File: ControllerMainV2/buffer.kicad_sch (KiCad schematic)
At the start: 21 parts

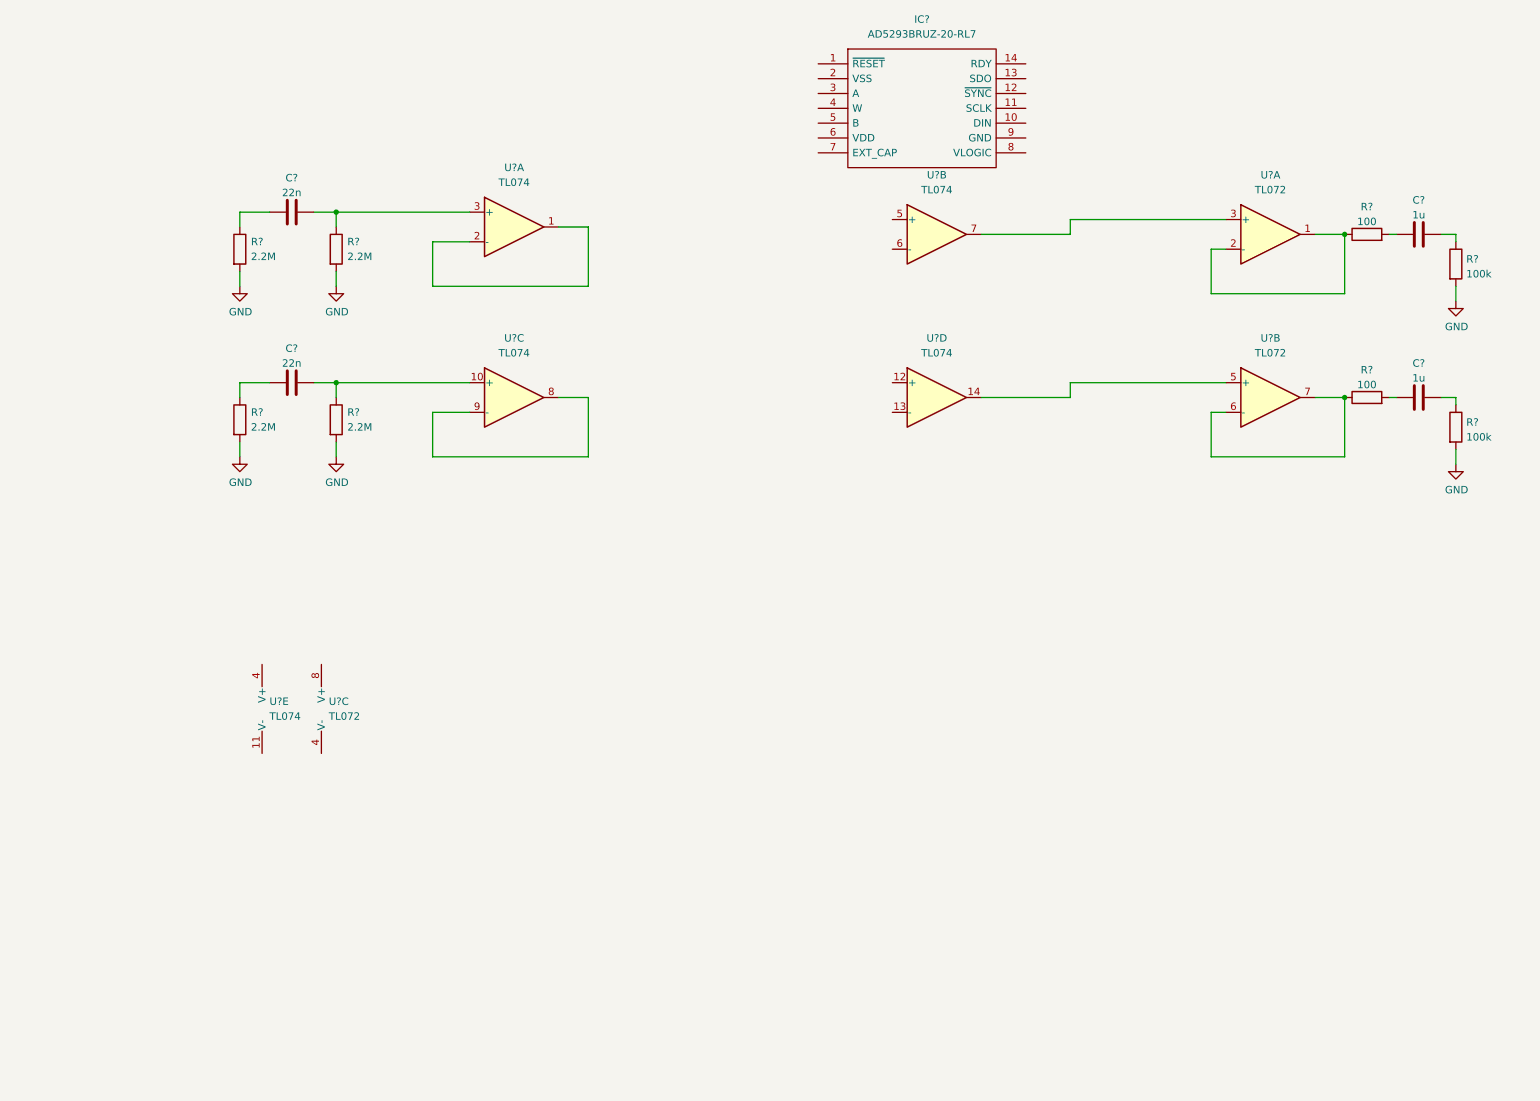
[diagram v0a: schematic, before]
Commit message: Added amp schematic
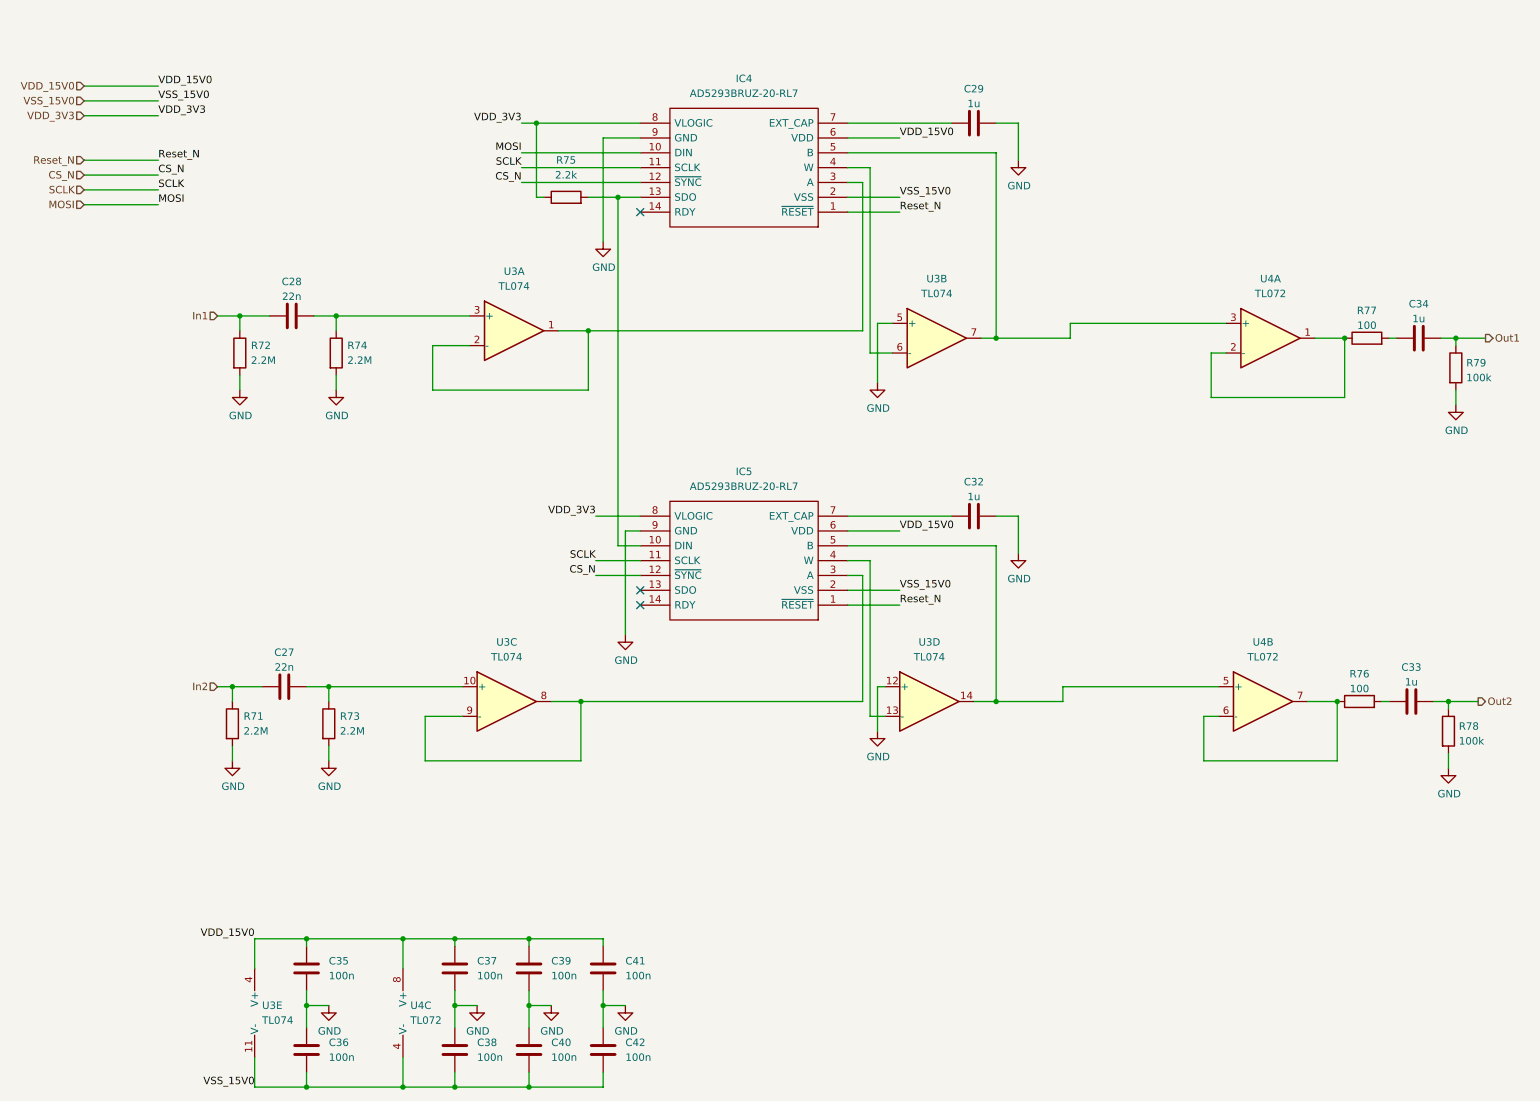
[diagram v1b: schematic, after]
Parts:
- added C29, C32: 1u, Capacitor_SMD:C_1206_3216Metric_Pad1.33x1.80mm_HandSolder, symbol Device:C
- added C35, C36, C37, C38, C39, C40, C41, C42: 100n, Capacitor_SMD:C_1206_3216Metric_Pad1.33x1.80mm_HandSolder, symbol Device:C
- added IC5: AD5293BRUZ-20-RL7, SOP65P640X120-14N, symbol SamacSys_Parts:AD5293BRUZ-20-RL7
- added R75: 2.2k, Resistor_SMD:R_1206_3216Metric_Pad1.30x1.75mm_HandSolder, symbol Device:R
- gave numbers to parts that had none: 15
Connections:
- net GND: now also IC4.9 (GND), U3.12 (+), U3.5 (+), C29.2, C32.2, C35.1, C36.2, C37.1, C38.2, C39.1, C40.2, C41.1, C42.2, IC5.9 (GND)
- net Out1: now reaches C34.2, R79.1
- net at U3.14, U4.5 (+): now also IC5.5 (B)
- net Out2: now reaches C33.2, R78.1
- net In2: now reaches C27.1, R71.1
- net at U3.6 (-): now also IC4.4 (W)
- net at U3.7, U4.3 (+): now also IC4.5 (B)
- net at U3.8, U3.9 (-): now also IC5.3 (A)
- net Reset_N: now reaches IC4.1 (~{RESET})
- net Reset_N: now also IC5.1 (~{RESET})
- net MOSI: now reaches IC4.10 (DIN)
- net SCLK: now reaches IC4.11 (SCLK)
- net SCLK: now also IC5.11 (SCLK)
- net CS_N: now reaches IC4.12 (~{SYNC})
- net CS_N: now also IC5.12 (~{SYNC})
- net at IC4.13 (SDO): now also IC5.10 (DIN), R75.2
- net VSS_15V0: now reaches IC4.2 (VSS)
- net VSS_15V0: now also U3.11 (V-), U4.4 (V-), C36.1, C38.1, C40.1, C42.1, IC5.2 (VSS)
- net at IC4.3 (A): now also U3.1, U3.2 (-)
- net VDD_15V0: now reaches IC4.6 (VDD)
- net VDD_15V0: now also U3.4 (V+), U4.8 (V+), C35.2, C37.2, C39.2, C41.2, IC5.6 (VDD)
- net at IC4.7 (EXT_CAP): now also C29.1
- net VDD_3V3: now reaches IC4.8 (VLOGIC)
- net VDD_3V3: now also IC5.8 (VLOGIC), R75.1
- net In1: now reaches C28.1, R72.1
- net at U3.13 (-): now also IC5.4 (W)
- new net: C32.1, IC5.7 (EXT_CAP)
- no-connect marks 0 -> 3
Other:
- moved on the sheet: C27, C28, C33, C34, IC4, R71, R72, R73, R74, R76, R77, R78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

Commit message: Layout of PGAs
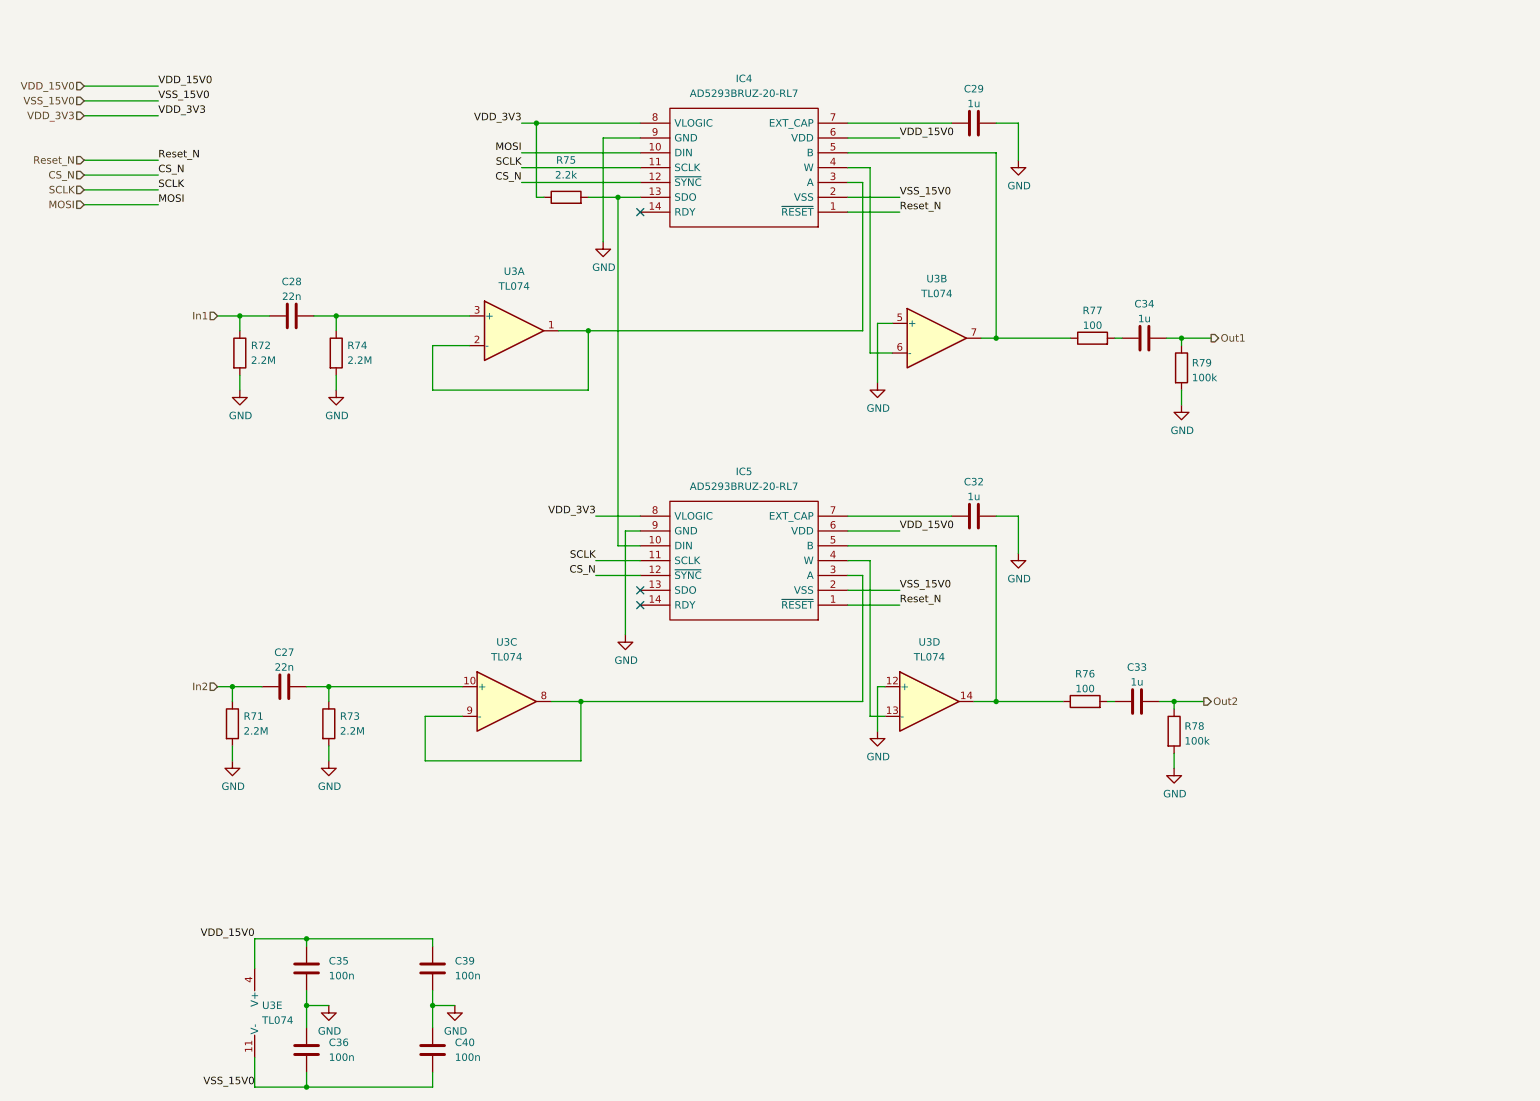
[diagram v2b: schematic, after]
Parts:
- removed C37, C38, C41, C42: 100n, Capacitor_SMD:C_1206_3216Metric_Pad1.33x1.80mm_HandSolder, symbol Device:C
- removed U4: TL072, symbol Amplifier_Operational:TL072
- IC4, IC5: footprint SOP65P640X120-14N -> SamacSys_Parts:SOP65P640X120-14N
- U3: footprint (none) -> SamacSys_Parts:SOIC127P600X175-14N
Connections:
- net at IC5.5 (B), U3.14: now also R76.1
- net at IC4.5 (B), U3.7: now also R77.1
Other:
- moved on the sheet: C33, C34, C39, C40, R76, R77, R78, R79
